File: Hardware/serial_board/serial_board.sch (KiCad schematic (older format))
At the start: 6 parts, among them J1 Conn_01x40, J2 Conn_01x06, U1 W65C51NxP, X1 CXO_DIP8

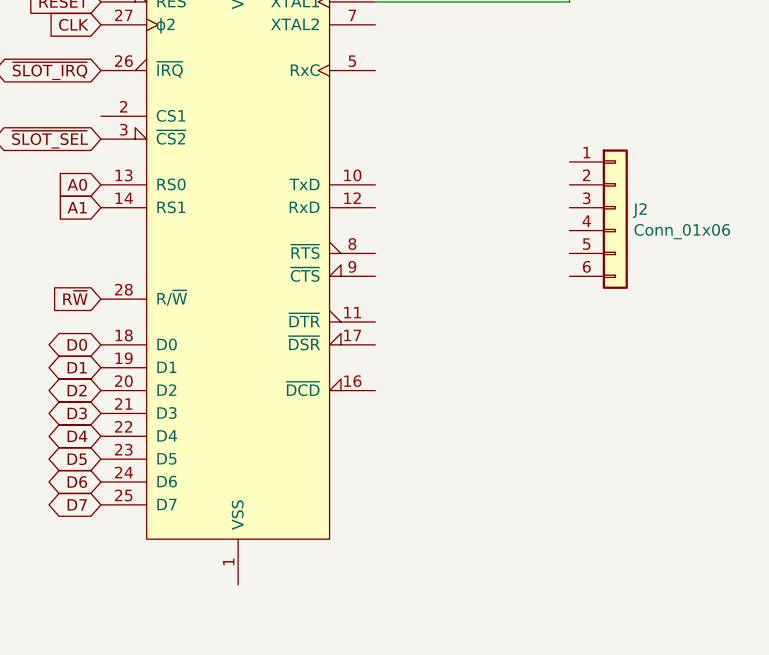
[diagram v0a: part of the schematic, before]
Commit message: USB serial adapter socket
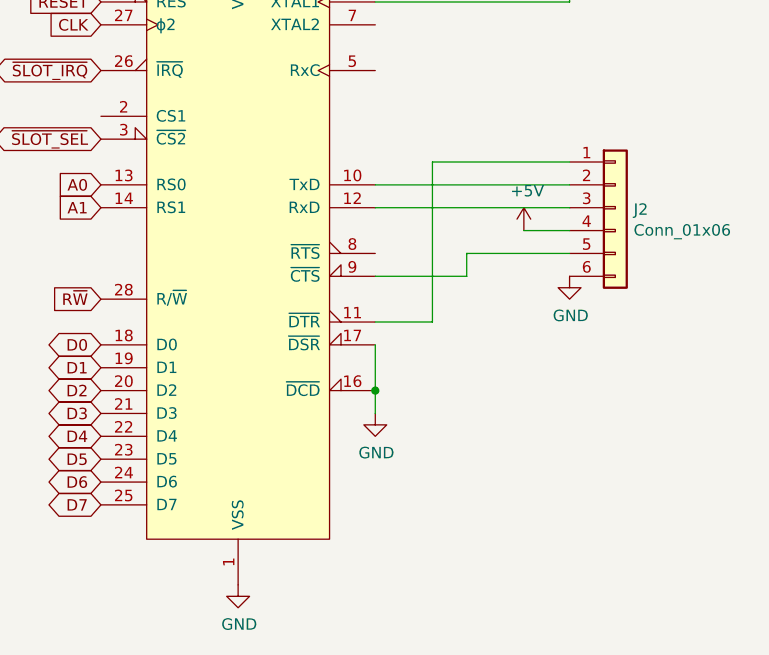
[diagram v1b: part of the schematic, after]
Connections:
- net +5V: now also J2.4 (Pin_4)
- net GND: now also J2.6 (Pin_6), U1.1 (VSS), U1.16 (~DCD), U1.17 (~DSR)
- net at U1.10 (TxD): now also J2.2 (Pin_2)
- net at U1.11 (~DTR): now also J2.1 (Pin_1)
- net at U1.12 (RxD): now also J2.3 (Pin_3)
- net at U1.9 (~CTS): now also J2.5 (Pin_5)
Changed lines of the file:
@@
 	1    0    0    -1
 $EndComp
+$Comp
+L power:GND #PWR?
+U 1 1 5FEDCBB9
+P 5300 5050
+F 0 "#PWR?" H 5300 4800 50  0001 C CNN
+F 1 "GND" H 5305 4877 50  0000 C CNN
+F 2 "" H 5300 5050 50  0001 C CNN
+F 3 "" H 5300 5050 50  0001 C CNN
+	1    5300 5050
+	1    0    0    -1
+$EndComp
+$Comp
+L power:GND #PWR?
+U 1 1 5FEDD20A
+P 6750 3700
+F 0 "#PWR?" H 6750 3450 50  0001 C CNN
+F 1 "GND" H 6755 3527 50  0000 C CNN
+F 2 "" H 6750 3700 50  0001 C CNN
+F 3 "" H 6750 3700 50  0001 C CNN
+	1    6750 3700
+	1    0    0    -1
+$EndComp
+Wire Wire Line
+	6750 3600 6300 3600
+Wire Wire Line
+	6300 3600 6300 3700
+Wire Wire Line
+	6300 3700 5900 3700
+$Comp
+L power:+5V #PWR?
+U 1 1 5FEDDFEF
+P 6550 3500
+F 0 "#PWR?" H 6550 3350 50  0001 C CNN
+F 1 "+5V" H 6565 3673 50  0000 C CNN
+F 2 "" H 6550 3500 50  0001 C CNN
+F 3 "" H 6550 3500 50  0001 C CNN
+	1    6550 3500
+	1    0    0    -1
+$EndComp
+Wire Wire Line
+	6750 3500 6550 3500
+Wire Wire Line
+	6750 3400 5900 3400
+Wire Wire Line
+	6750 3300 5900 3300
+Wire Wire Line
+	6750 3200 6150 3200
+Wire Wire Line
+	6150 3200 6150 3900
+Wire Wire Line
+	6150 3900 5900 3900
+$Comp
+L power:GND #PWR?
+U 1 1 5FEDFB28
+P 5900 4300
+F 0 "#PWR?" H 5900 4050 50  0001 C CNN
+F 1 "GND" H 5905 4127 50  0000 C CNN
+F 2 "" H 5900 4300 50  0001 C CNN
+F 3 "" H 5900 4300 50  0001 C CNN
+	1    5900 4300
+	1    0    0    -1
+$EndComp
+Wire Wire Line
+	5900 4000 5900 4200
+Connection ~ 5900 4200
+Wire Wire Line
+	5900 4200 5900 4300
 $EndSCHEMATC

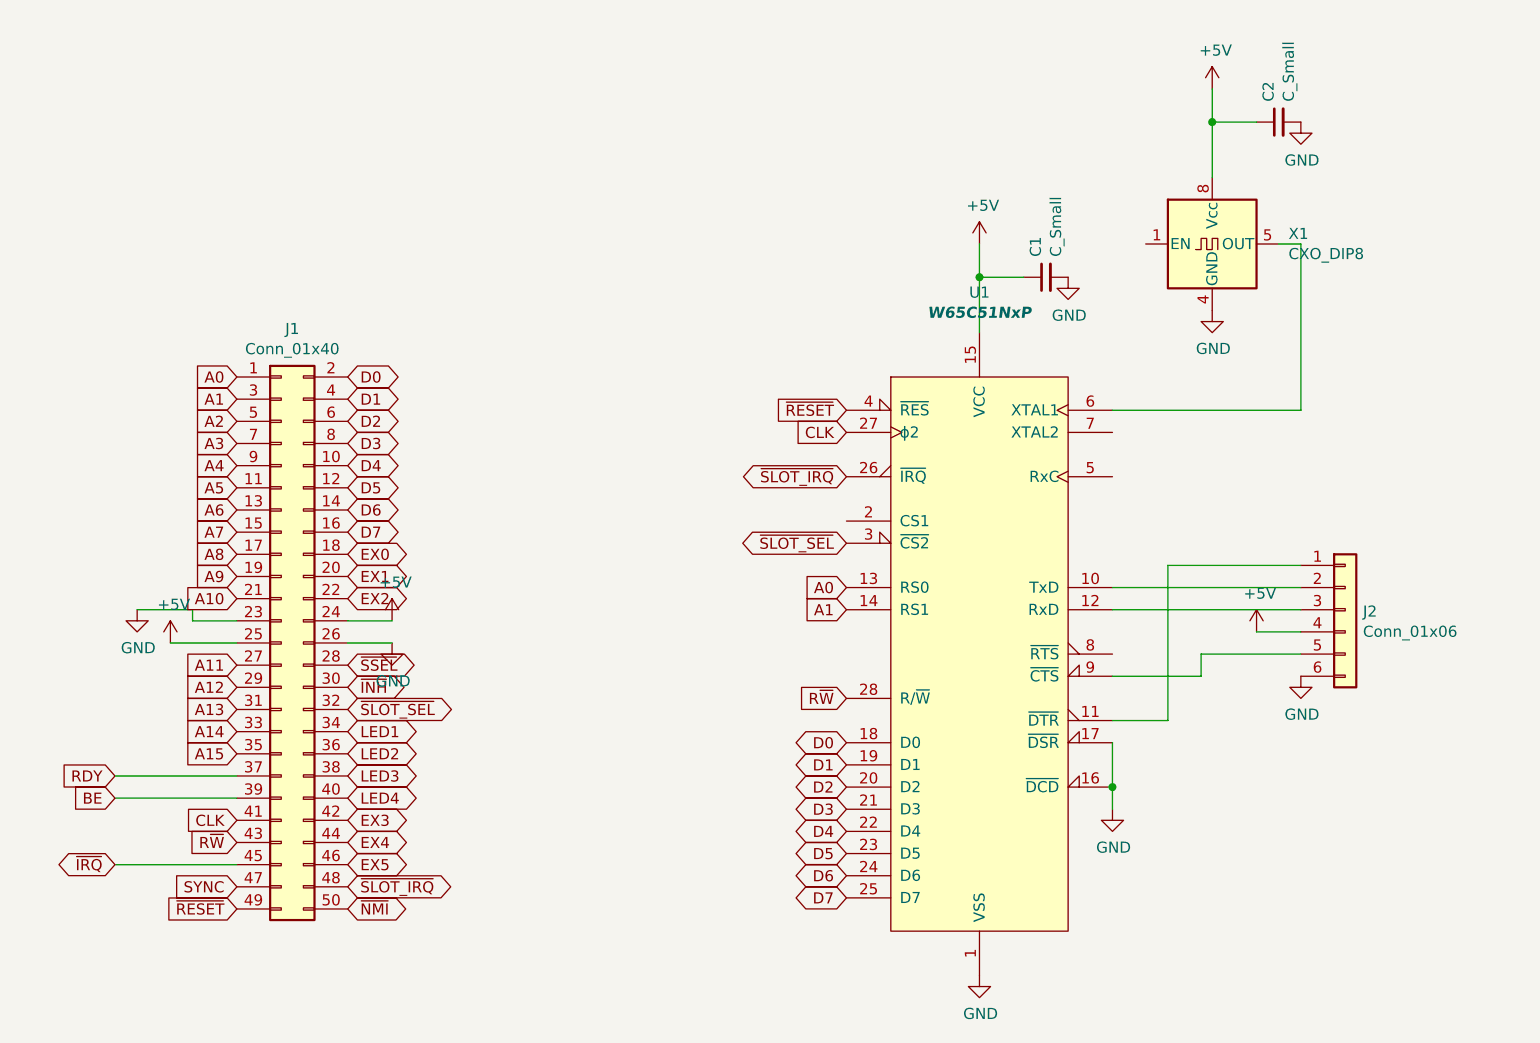
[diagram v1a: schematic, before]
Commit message: Many updates. SLOW signal is now shared amongst all slots, so their output has to be open drain.
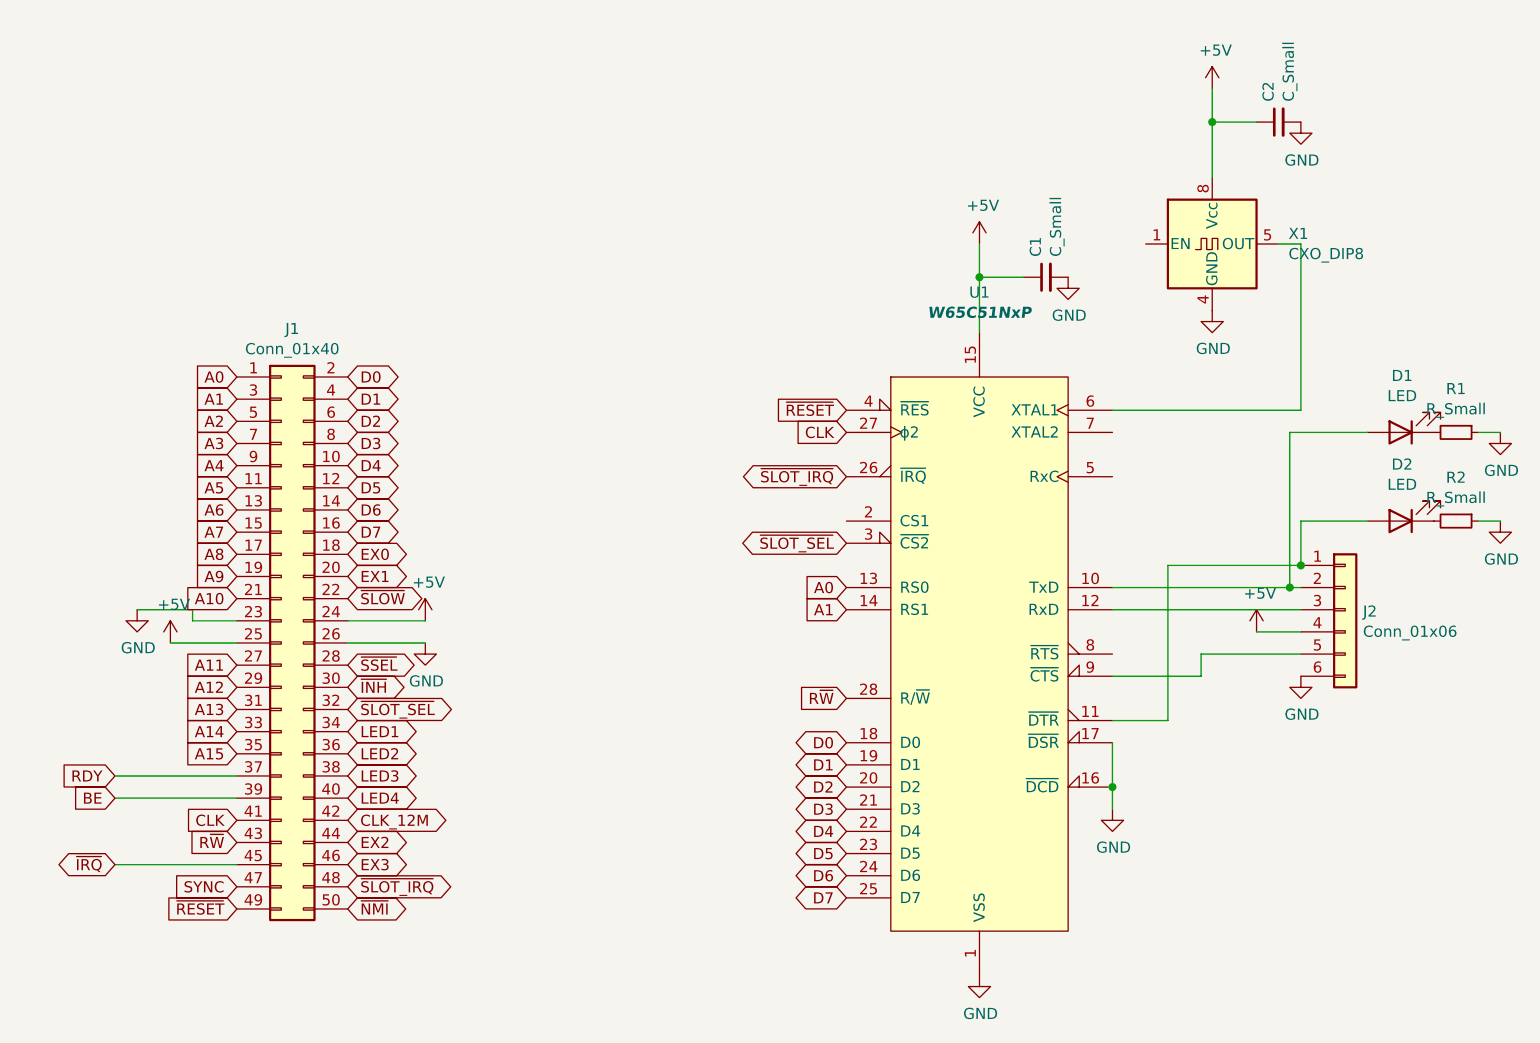
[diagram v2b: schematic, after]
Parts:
- added D1, D2: LED, LED_SMD:LED_1206_3216Metric_Pad1.42x1.75mm_HandSolder, symbol Device:LED
- added R1, R2: R_Small, Resistor_SMD:R_0805_2012Metric_Pad1.15x1.40mm_HandSolder, symbol Device:R_Small
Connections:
- net EX4 is gone; now on net EX2: J1.44 (Pin_44)
- net EX5 is gone; now on net EX3: J1.46 (Pin_46)
- net EX2: no longer J1.22 (Pin_22)
- net EX3: no longer J1.42 (Pin_42)
- net GND: now also R1.1, R2.1
- net at J2.2 (Pin_2), U1.10 (TxD): now also D1.2 (A)
- net at J2.1 (Pin_1), U1.11 (~DTR): now also D2.2 (A)
- new net: D1.1 (K), R1.2
- new net: D2.1 (K), R2.2
- new net CLK_12M: J1.42 (Pin_42)
- new net ~SLOW~: J1.22 (Pin_22)
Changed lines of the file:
@@
 L power:+5V #PWR0101
 U 1 1 5FD64472
-P 2650 3450
-F 0 "#PWR0101" H 2650 3300 50  0001 C CNN
-F 1 "+5V" H 2665 3623 50  0000 C CNN
-F 2 "" H 2650 3450 50  0001 C CNN
-F 3 "" H 2650 3450 50  0001 C CNN
-	1    2650 3450
-	1    0    0    -1
-$EndComp
-Wire Wire Line
-	2650 3450 2450 3450
+P 2800 3450
+F 0 "#PWR0101" H 2800 3300 50  0001 C CNN
+F 1 "+5V" H 2815 3623 50  0000 C CNN
+F 2 "" H 2800 3450 50  0001 C CNN
+F 3 "" H 2800 3450 50  0001 C CNN
+	1    2800 3450
+	1    0    0    -1
+$EndComp
+Wire Wire Line
+	2800 3450 2450 3450
 $Comp
 L power:+5V #PWR0102
@@
 L power:GND #PWR0103
 U 1 1 5FD65E00
-P 2650 3550
-F 0 "#PWR0103" H 2650 3300 50  0001 C CNN
-F 1 "GND" H 2655 3377 50  0000 C CNN
-F 2 "" H 2650 3550 50  0001 C CNN
-F 3 "" H 2650 3550 50  0001 C CNN
-	1    2650 3550
-	1    0    0    -1
-$EndComp
-Wire Wire Line
-	2650 3550 2450 3550
+P 2800 3550
+F 0 "#PWR0103" H 2800 3300 50  0001 C CNN
+F 1 "GND" H 2805 3377 50  0000 C CNN
+F 2 "" H 2800 3550 50  0001 C CNN
+F 3 "" H 2800 3550 50  0001 C CNN
+	1    2800 3550
+	1    0    0    -1
+$EndComp
+Wire Wire Line
+	2800 3550 2450 3550
 $Comp
 L power:GND #PWR0104
@@
 ~SLOT_IRQ~
 Text GLabel 2450 4550 2    50   BiDi ~ 0
-EX5
+EX3
 Text GLabel 2450 4450 2    50   BiDi ~ 0
-EX4
-Text GLabel 2450 4350 2    50   BiDi ~ 0
-EX3
+EX2
 $Comp
 L Device:C_Small C1
@@
 EX1
 Text GLabel 2450 3350 2    50   BiDi ~ 0
-EX2
+~SLOW~
 $Comp
 L 65xx:W65C51NxP U1
@@
 $EndComp
 $Comp
-L power:GND #PWR?
+L power:GND #PWR0110
 U 1 1 5FEDCBB9
 P 5300 5050
-F 0 "#PWR?" H 5300 4800 50  0001 C CNN
+F 0 "#PWR0110" H 5300 4800 50  0001 C CNN
 F 1 "GND" H 5305 4877 50  0000 C CNN
 F 2 "" H 5300 5050 50  0001 C CNN
@@
 $EndComp
 $Comp
-L power:GND #PWR?
+L power:GND #PWR0111
 U 1 1 5FEDD20A
 P 6750 3700
-F 0 "#PWR?" H 6750 3450 50  0001 C CNN
+F 0 "#PWR0111" H 6750 3450 50  0001 C CNN
 F 1 "GND" H 6755 3527 50  0000 C CNN
 F 2 "" H 6750 3700 50  0001 C CNN
@@
 	6300 3700 5900 3700
 $Comp
-L power:+5V #PWR?
+L power:+5V #PWR0112
 U 1 1 5FEDDFEF
 P 6550 3500
-F 0 "#PWR?" H 6550 3350 50  0001 C CNN
+F 0 "#PWR0112" H 6550 3350 50  0001 C CNN
 F 1 "+5V" H 6565 3673 50  0000 C CNN
 F 2 "" H 6550 3500 50  0001 C CNN
@@
 	6750 3400 5900 3400
 Wire Wire Line
-	6750 3300 5900 3300
+	6750 3300 6700 3300
 Wire Wire Line
 	6750 3200 6150 3200
@@
 	6150 3900 5900 3900
 $Comp
-L power:GND #PWR?
+L power:GND #PWR0113
 U 1 1 5FEDFB28
 P 5900 4300
-F 0 "#PWR?" H 5900 4050 50  0001 C CNN
+F 0 "#PWR0113" H 5900 4050 50  0001 C CNN
 F 1 "GND" H 5905 4127 50  0000 C CNN
 F 2 "" H 5900 4300 50  0001 C CNN
@@
 Wire Wire Line
 	5900 4200 5900 4300
+Text GLabel 2450 4350 2    50   BiDi ~ 0
+CLK_12M
+$Comp
+L Device:LED D1
+U 1 1 5FFE4203
+P 7200 2600
+F 0 "D1" H 7193 2345 50  0000 C CNN
+F 1 "LED" H 7193 2436 50  0000 C CNN
+F 2 "LED_SMD:LED_1206_3216Metric_Pad1.42x1.75mm_HandSolder" H 7200 2600 50  0001 C CNN
+F 3 "~" H 7200 2600 50  0001 C CNN
+	1    7200 2600
+	-1   0    0    1
+$EndComp
+$Comp
+L Device:R_Small R1
+U 1 1 5FFE6639
+P 7450 2600
+F 0 "R1" V 7254 2600 50  0000 C CNN
+F 1 "R_Small" V 7345 2600 50  0000 C CNN
+F 2 "Resistor_SMD:R_0805_2012Metric_Pad1.15x1.40mm_HandSolder" H 7450 2600 50  0001 C CNN
+F 3 "~" H 7450 2600 50  0001 C CNN
+	1    7450 2600
+	0    1    1    0
+$EndComp
+Wire Wire Line
+	7050 2600 6700 2600
+Wire Wire Line
+	6700 2600 6700 3300
+Connection ~ 6700 3300
+Wire Wire Line
+	6700 3300 5900 3300
+$Comp
+L power:GND #PWR0114
+U 1 1 5FFE7630
+P 7650 2600
+F 0 "#PWR0114" H 7650 2350 50  0001 C CNN
+F 1 "GND" H 7655 2427 50  0000 C CNN
+F 2 "" H 7650 2600 50  0001 C CNN
+F 3 "" H 7650 2600 50  0001 C CNN
+	1    7650 2600
+	1    0    0    -1
+$EndComp
+Wire Wire Line
+	7650 2600 7550 2600
+$Comp
+L Device:LED D2
+U 1 1 5FFE96CA
+P 7200 3000
+F 0 "D2" H 7193 2745 50  0000 C CNN
+F 1 "LED" H 7193 2836 50  0000 C CNN
+F 2 "LED_SMD:LED_1206_3216Metric_Pad1.42x1.75mm_HandSolder" H 7200 3000 50  0001 C CNN
+F 3 "~" H 7200 3000 50  0001 C CNN
+	1    7200 3000
+	-1   0    0    1
+$EndComp
+$Comp
+L Device:R_Small R2
+U 1 1 5FFE96D0
+P 7450 3000
+F 0 "R2" V 7254 3000 50  0000 C CNN
+F 1 "R_Small" V 7345 3000 50  0000 C CNN
+F 2 "Resistor_SMD:R_0805_2012Metric_Pad1.15x1.40mm_HandSolder" H 7450 3000 50  0001 C CNN
+F 3 "~" H 7450 3000 50  0001 C CNN
+	1    7450 3000
+	0    1    1    0
+$EndComp
+$Comp
+L power:GND #PWR0115
+U 1 1 5FFE96D7
+P 7650 3000
+F 0 "#PWR0115" H 7650 2750 50  0001 C CNN
+F 1 "GND" H 7655 2827 50  0000 C CNN
+F 2 "" H 7650 3000 50  0001 C CNN
+F 3 "" H 7650 3000 50  0001 C CNN
+	1    7650 3000
+	1    0    0    -1
+$EndComp
+Wire Wire Line
+	7650 3000 7550 3000
+Wire Wire Line
+	7050 3000 6750 3000
+Wire Wire Line
+	6750 3000 6750 3200
+Connection ~ 6750 3200
 $EndSCHEMATC

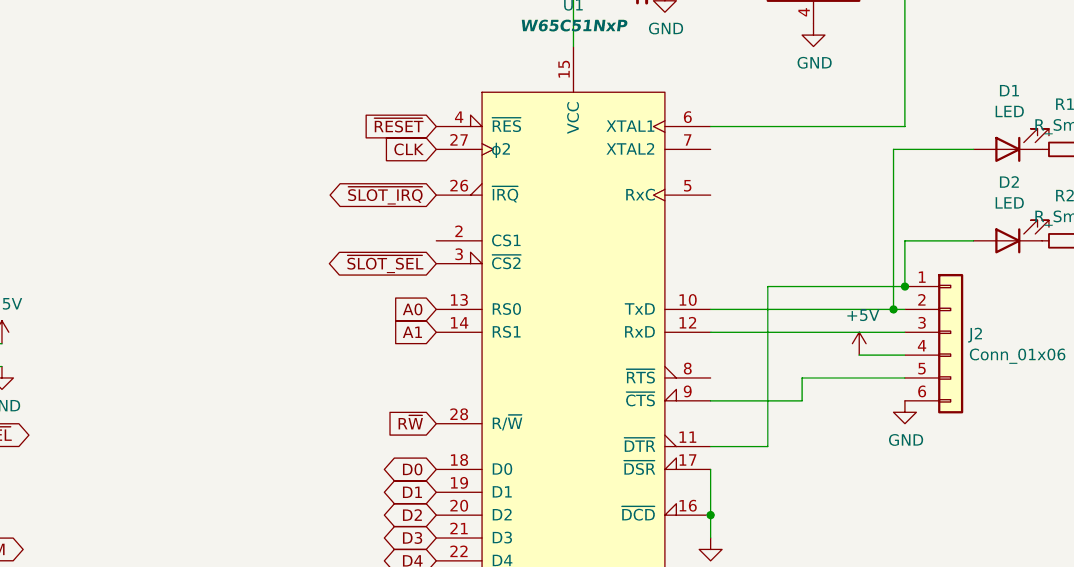
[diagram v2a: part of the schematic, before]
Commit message: Add pullup on CS1 and move cts line to RTS of 6551
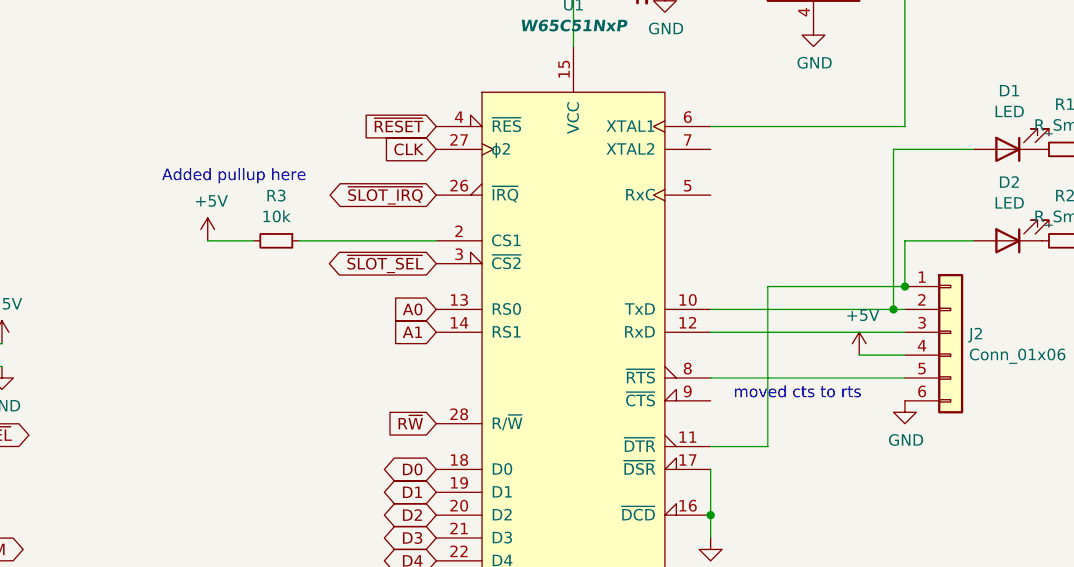
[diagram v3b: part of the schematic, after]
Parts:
- added R3: 10k, Resistor_SMD:R_0805_2012Metric_Pad1.15x1.40mm_HandSolder, symbol Device:R_Small
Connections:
- net +5V: now also R3.2
- net at U1.2 (CS1): now also R3.1
- net at U1.8 (~RTS): now also J2.5 (Pin_5)
- net at U1.9 (~CTS): no longer J2.5 (Pin_5)
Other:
- note added: "Added pullup here"
- note added: "moved cts to rts"
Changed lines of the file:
@@
 	1    0    0    -1
 $EndComp
-Wire Wire Line
-	6750 3600 6300 3600
-Wire Wire Line
-	6300 3600 6300 3700
-Wire Wire Line
-	6300 3700 5900 3700
 $Comp
 L power:+5V #PWR0112
@@
 	6750 3000 6750 3200
 Connection ~ 6750 3200
+$Comp
+L Device:R_Small R3
+U 1 1 60353899
+P 4000 3000
+F 0 "R3" V 3804 3000 50  0000 C CNN
+F 1 "10k" V 3895 3000 50  0000 C CNN
+F 2 "Resistor_SMD:R_0805_2012Metric_Pad1.15x1.40mm_HandSolder" H 4000 3000 50  0001 C CNN
+F 3 "~" H 4000 3000 50  0001 C CNN
+	1    4000 3000
+	0    1    1    0
+$EndComp
+Wire Wire Line
+	4700 3000 4100 3000
+$Comp
+L power:+5V #PWR0116
+U 1 1 60354CFE
+P 3700 3000
+F 0 "#PWR0116" H 3700 2850 50  0001 C CNN
+F 1 "+5V" H 3715 3173 50  0000 C CNN
+F 2 "" H 3700 3000 50  0001 C CNN
+F 3 "" H 3700 3000 50  0001 C CNN
+	1    3700 3000
+	1    0    0    -1
+$EndComp
+Wire Wire Line
+	3900 3000 3700 3000
+Text Notes 3500 2750 0    50   ~ 0
+Added pullup here
+Wire Wire Line
+	5900 3600 6750 3600
+Text Notes 6000 3700 0    50   ~ 0
+moved cts to rts
 $EndSCHEMATC

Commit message: small fixes on the hardware
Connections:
- net at J2.1 (Pin_1), U1.11 (~DTR): no longer D2.2 (A)
- net at J2.3 (Pin_3), U1.12 (RxD): now also D2.2 (A)
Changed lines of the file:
@@
 	6750 3500 6550 3500
 Wire Wire Line
-	6750 3400 5900 3400
+	6750 3400 6450 3400
 Wire Wire Line
 	6750 3300 6700 3300
@@
 Wire Wire Line
 	7650 3000 7550 3000
-Wire Wire Line
-	7050 3000 6750 3000
-Wire Wire Line
-	6750 3000 6750 3200
-Connection ~ 6750 3200
 $Comp
 L Device:R_Small R3
@@
 Text Notes 6000 3700 0    50   ~ 0
 moved cts to rts
+Wire Wire Line
+	6450 3000 6450 3400
+Wire Wire Line
+	6450 3000 7050 3000
+Connection ~ 6450 3400
+Wire Wire Line
+	6450 3400 5900 3400
 $EndSCHEMATC

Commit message: update serial board
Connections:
- net GND: now also U1.11 (~DTR), U1.9 (~CTS); no longer U1.17 (~DSR)
- net TX: now reaches D1.2 (A), J2.2 (Pin_2), U1.10 (TxD)
- net ~DSR~: now reaches J2.1 (Pin_1)
- net ~DSR~: now also U1.17 (~DSR); no longer U1.11 (~DTR)
- net RX: now reaches D2.2 (A), J2.3 (Pin_3), U1.12 (RxD)
- net ~RTS~: now reaches J2.5 (Pin_5), U1.8 (~RTS)
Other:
- note removed: "moved cts to rts"
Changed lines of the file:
@@
 Wire Wire Line
 	6750 3200 6150 3200
-Wire Wire Line
-	6150 3200 6150 3900
-Wire Wire Line
-	6150 3900 5900 3900
 $Comp
 L power:GND #PWR0113
@@
 	1    0    0    -1
 $EndComp
-Wire Wire Line
-	5900 4000 5900 4200
-Connection ~ 5900 4200
 Wire Wire Line
 	5900 4200 5900 4300
@@
 Wire Wire Line
 	5900 3600 6750 3600
-Text Notes 6000 3700 0    50   ~ 0
-moved cts to rts
 Wire Wire Line
 	6450 3000 6450 3400
@@
 Wire Wire Line
 	6450 3400 5900 3400
+Text Label 5900 3300 0    50   ~ 0
+TX
+Text Label 5900 3400 0    50   ~ 0
+RX
+Text Label 5900 3600 0    50   ~ 0
+~RTS~
+Text Label 5900 3700 0    50   ~ 0
+~CTS~
+Text Label 5900 3900 0    50   ~ 0
+~DTR~
+Text Label 5900 4000 0    50   ~ 0
+~DSR~
+Text Label 5900 4200 0    50   ~ 0
+~DCD~
+Wire Wire Line
+	5900 3700 6050 3700
+Wire Wire Line
+	6150 3200 6150 4000
+Wire Wire Line
+	5900 4000 6150 4000
+Wire Wire Line
+	5900 3900 6050 3900
+Wire Wire Line
+	6050 3900 6050 3700
+Wire Wire Line
+	6050 3900 6050 4200
+Wire Wire Line
+	6050 4200 5900 4200
+Connection ~ 6050 3900
+Connection ~ 5900 4200
 $EndSCHEMATC
